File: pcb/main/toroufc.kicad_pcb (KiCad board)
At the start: 2 copper layers, 74.8 x 94.7 mm, 43 parts, among them J1 HAT, J10 RPAD, J11 POT1-3, J12 POT4-6, J13 REN1, J14 REN2, J15 I2C, J16 Conn_01x04_Male, J2 RKR1-2, J3 RKR3-4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

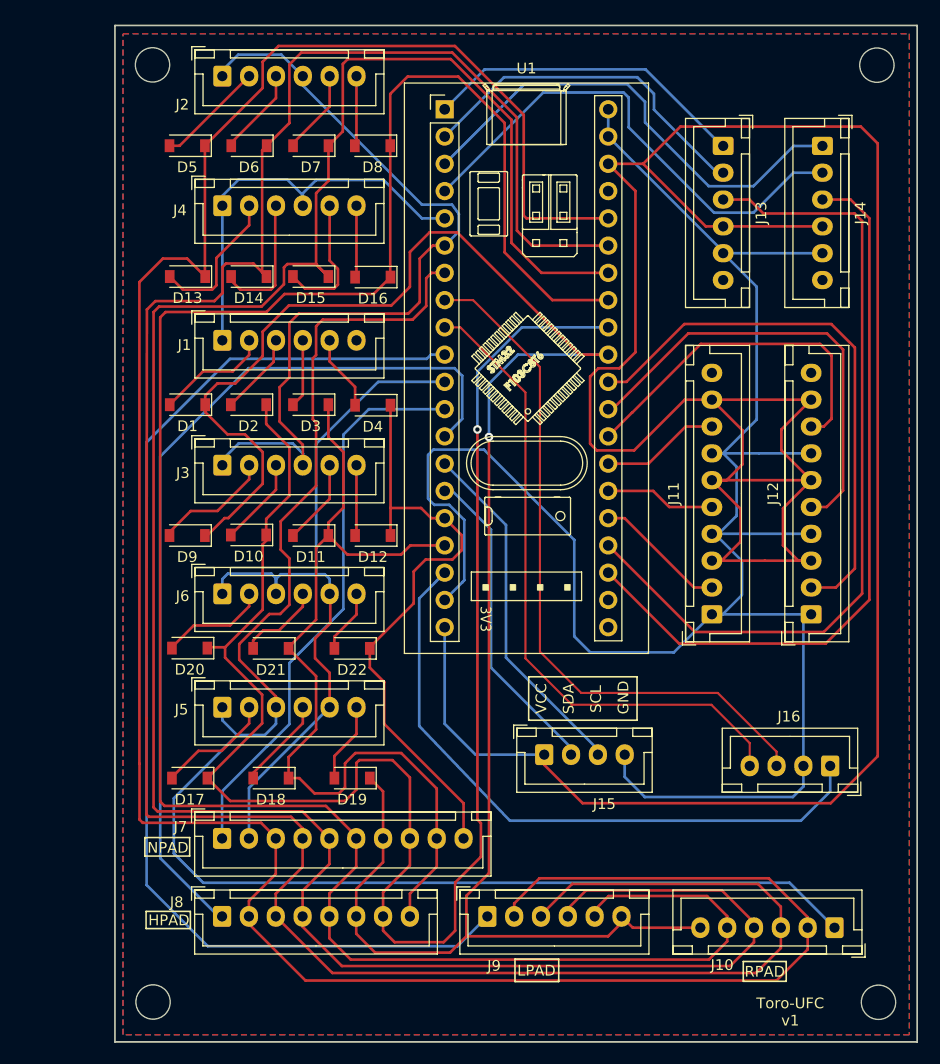
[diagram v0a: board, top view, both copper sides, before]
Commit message: Added test points, reduced size, removed i2c, labels, bluepill fix.
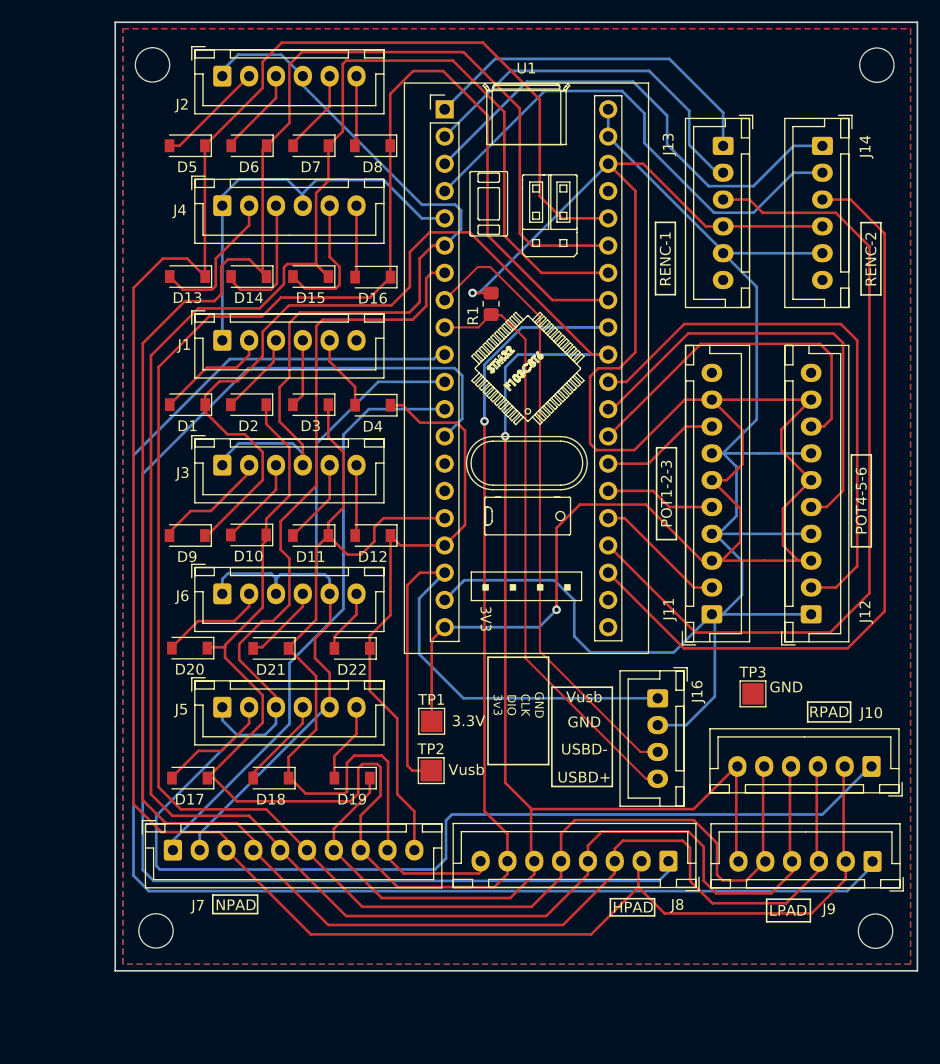
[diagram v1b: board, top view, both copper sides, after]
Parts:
- removed J15: I2C, Connector_JST:JST_XH_B4B-XH-A_1x04_P2.50mm_Vertical
- added R1: R1.5K, Resistor_SMD:R_0805_2012Metric_Pad1.20x1.40mm_HandSolder, F.Cu at (144.5, 75.6)
- added TP1: VCC, TestPoint:TestPoint_Pad_2.0x2.0mm, F.Cu at (139.0, 114.5)
- added TP2: Vusb, TestPoint:TestPoint_Pad_2.0x2.0mm, F.Cu at (138.9, 119.1)
- added TP3: GND, TestPoint:TestPoint_Pad_2.0x2.0mm, F.Cu at (168.9, 112.0)
- J16: value Conn_01x04_Male -> USB connector
- moved J8 41.9 mm to (161.1, 127.6), turned to 180 degrees
- moved J9 36.3 mm to (180.1, 127.6), turned to 180 degrees
- moved J16 17.3 mm to (160.1, 112.4), turned to -90 degrees
- moved J10 15.4 mm to (180.0, 118.8)
- moved REF** 6.63 mm to (180.3, 134.1)
- moved REF** 6.63 mm to (113.3, 134.1)
- moved J7 4.71 mm to (114.9, 126.5)
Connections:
- U1 pad 16: /ROW8 -> /ROW7
- U1 pad 17: /ROW7 -> /ROW8
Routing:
- net VCC: track 270.6 -> 190.4 mm, vias 0 -> 2
- net GND: track 192.0 -> 144.2 mm
- net /COL1: track 83.6 -> 128.1 mm
- net /COL4: track 107.7 -> 142.9 mm
- net /SCL: track 33.0 -> 0.00 mm
- net /SDA: track 29.9 -> 0.00 mm
- net /ROW1: track 237.0 -> 213.2 mm
- net /ROW2: track 229.6 -> 213.2 mm
- net /ROW3: track 220.1 -> 208.0 mm
- net /COL5: track 143.6 -> 153.7 mm
- net /ROW4: track 207.2 -> 198.6 mm
- net /ROW6: track 156.9 -> 148.8 mm
- net /USBD-: track 65.2 -> 58.1 mm
- net /USBD+: track 61.1 -> 55.7 mm
- net /Vusb: track 60.8 -> 55.7 mm
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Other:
- board size 74.8 x 94.7 mm -> 74.8 x 88.4 mm
- board text added: "3.3V"
- board text added: "GND CLK DIO 3v3"
- board text added: "POT1-2-3"
- board text added: "POT4-5-6"
- board text added: "RENC-1"
- board text added: "RENC-2"
- board text added: "Toro-UFC v1 2022"
- board text added: "USBD+"
- board text added: "USBD-"
- board text added: "Vusb"
- board text removed: "SCL"
- board text removed: "SDA"
- board text removed: "Toro-UFC v1"
- board text removed: "VCC"

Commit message: First production
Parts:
- moved D11 9.64 mm to (119.0, 101.5)
- moved D3 9.64 mm to (119.0, 89.3)
- moved D15 9.64 mm to (119.0, 77.3)
- moved J9 9.64 mm to (171.4, 131.8)
- moved REF** 9.64 mm to (171.7, 138.3)
- moved REF** 9.64 mm to (104.6, 138.3)
- moved D1 9.64 mm to (107.6, 89.3)
- moved D12 9.64 mm to (124.8, 101.5)
- moved D16 9.64 mm to (124.8, 77.4)
- moved D17 9.64 mm to (107.8, 124.1)
- moved D18 9.64 mm to (115.3, 124.1)
- moved D19 9.64 mm to (122.9, 124.1)
- moved D2 9.64 mm to (113.3, 89.3)
- moved D20 9.64 mm to (107.8, 111.9)
- moved D21 9.64 mm to (115.3, 112.0)
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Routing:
- net /ROW2: track 213.2 -> 209.7 mm
- net GND: track 144.2 -> 141.1 mm
- net /POT6: track 52.2 -> 49.3 mm
- net /ROW4: track 198.6 -> 195.8 mm
- net /ROW3: track 208.0 -> 205.2 mm
- net /COL4: track 142.9 -> 140.2 mm
- net /POT5: track 42.5 -> 40.1 mm
- net /COL1: track 128.1 -> 125.7 mm
- net /ROW5: track 188.2 -> 190.4 mm
- net /POT4: track 32.9 -> 30.9 mm
- net VCC: track 190.4 -> 188.8 mm
- net /Vusb: track 55.7 -> 54.1 mm
- net /REN1C: track 33.1 -> 31.7 mm
- net /COL6: track 78.3 -> 77.1 mm
- net /USBD-: track 58.1 -> 57.0 mm
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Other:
- board text added: "3v3 DIO CLK GND"
- board text added: "UFC-MAIN v1 2022"
- board text removed: "GND CLK DIO 3v3"
- board text removed: "Toro-UFC v1 2022"
